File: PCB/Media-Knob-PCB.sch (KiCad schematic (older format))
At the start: 0 parts

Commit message: Audio Switch eindesignt
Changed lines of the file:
@@
 F12 "SW2" I R 8450 4050 50
 F13 "SW1" I R 8450 3950 50
+F14 "Input_Select" O R 8450 5300 39
+F15 "Output_Select" O R 8450 5400 39
 $EndSheet
 $Sheet
@@
 Text Notes 9500 5350 0    50   ~ 0
 Auxiliary Switching\n
+Wire Wire Line
+	8450 5300 8650 5300
+Wire Wire Line
+	8450 5400 8650 5400
 $EndSCHEMATC

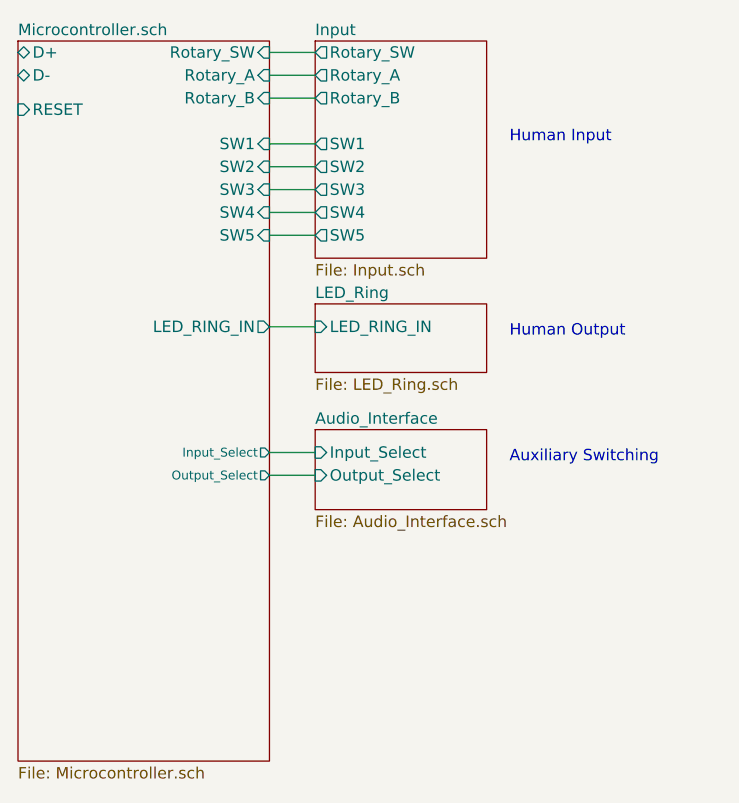
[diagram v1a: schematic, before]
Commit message: Sheet USB
USB Switch und USB Input Stecker hinzugefügt
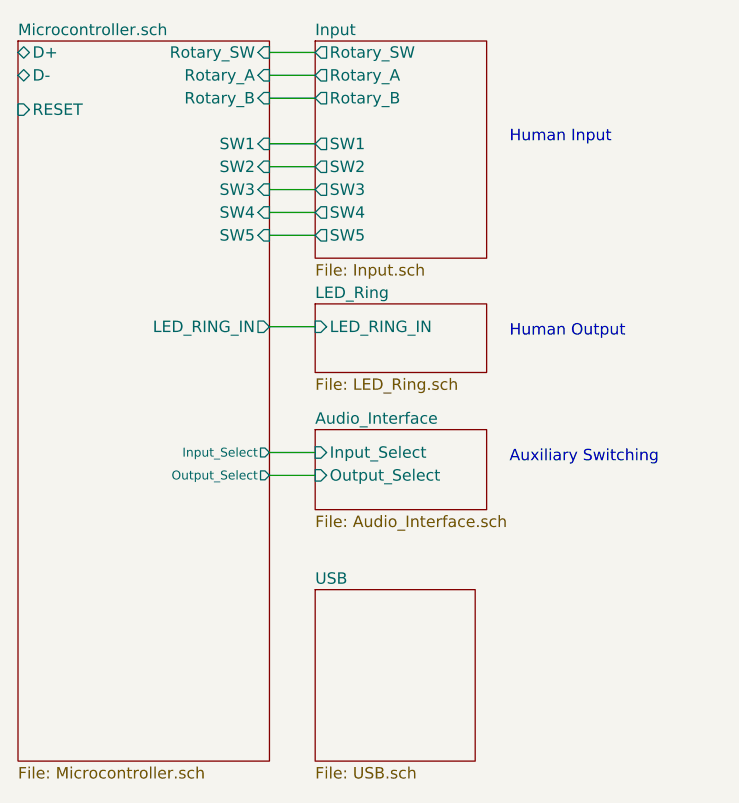
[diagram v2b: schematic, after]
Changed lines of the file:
@@
 $Descr A3 16535 11693
 encoding utf-8
-Sheet 1 5
+Sheet 1 6
 Title "Media-Knob"
 Date "2020-11-08"
@@
 Wire Wire Line
 	8450 5400 8650 5400
+$Sheet
+S 8650 5900 700  750
+U 5FBE9AF7
+F0 "USB" 50
+F1 "USB.sch" 50
+$EndSheet
 $EndSCHEMATC
